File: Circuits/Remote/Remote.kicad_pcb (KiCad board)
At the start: 2 copper layers, 80 x 68.1 mm, 31 parts, among them P1 WRITER, Q1 2SK4017, SW1 WakeUp, U1 TWE_LITE_DIP, U2 STEPUPDIP3.3V, U3 ATP3011-PU, U4 HT82V739

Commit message: Assigned footprint.
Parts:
- removed P1: WRITER, SIL-6
- added CN1: WRITER, SIL-6, F.Cu at (31.8, 73.7)
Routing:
- net GND: track 0.00 -> 143.4 mm
- net /QGND: track 20.3 -> 161.5 mm
- net VCC: track 0.00 -> 119.7 mm
- net /SDA: track 0.00 -> 78.8 mm
- net /RESET#: track 0.00 -> 72.1 mm
- net /SCL: track 0.00 -> 68.1 mm
- net /3.3V: track 15.2 -> 82.8 mm
- net /SPK-: track 0.00 -> 45.3 mm
- net /SPK+: track 0.00 -> 44.6 mm
- net /RXD: track 0.00 -> 43.8 mm
- net /CFG: track 0.00 -> 40.0 mm
- net N-000004: track 0.00 -> 39.5 mm
- net N-0000050: track 0.00 -> 37.5 mm
- net /RST: track 0.00 -> 35.6 mm
- net /PRG: track 0.00 -> 34.2 mm
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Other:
- net class power added: clearance 0.254, trace_width 0.508, via_dia 0.889, via_drill 0.635

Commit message: Consider NTH.
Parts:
- added PB-SGM-135: VAL**, PB-SGM-135, F.Cu at (57.1, 45.1)
- added R11: 10k, R4, F.Cu at (45.7, 58.4)
- RV1, RV2: footprint POT_CMS -> RV2
- moved SW1 41.9 mm to (36.8, 19.1), turned to 180 degrees
- moved BT1 34.1 mm to (99.1, 61.0), turned to 270 degrees
- moved C4 23.4 mm to (91.4, 53.3), turned to 0 degrees
- moved U4 13.7 mm to (91.4, 44.5)
- moved C6 12.7 mm to (91.4, 33.0)
- moved U1 10.2 mm to (33.0, 47.0)
- moved SP1 10.2 mm to (66.0, 19.1)
- moved C5 10.2 mm to (81.2, 69.3)
- moved LD1 10.2 mm to (45.6, 41.4)
- moved LD2 10.2 mm to (53.2, 41.4)
- moved LD3 10.2 mm to (60.8, 41.4)
- moved R1 10.2 mm to (45.6, 36.3)
- moved R2 10.2 mm to (53.2, 36.3)
- moved R3 10.2 mm to (60.8, 36.3)
- moved R4 10.2 mm to (53.2, 61.7)
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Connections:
- net N-000001 renamed /V0
- net N-0000021 renamed /LPF2
- net N-0000022 renamed /LPF1
- net N-0000023 renamed /AOUT
- net N-0000025 renamed /VOL
- net N-0000027 renamed /PLAY#
- net N-0000029 renamed /VREF
- net N-000003 renamed /PWM4
- net N-0000030 renamed /AudioIn
- net N-0000031 renamed /PWM2
- net N-000004 renamed /3V_Gate
- net N-000005 renamed /LD1
- net N-0000050 renamed /PWM1
- net N-000006 renamed /LD2
- net N-000007 renamed /LD3
- net N-000009 renamed /G
- R10 pad 2: N-0000020 -> /LPF3
- RV2 pad 1: /QGND -> /LPF3
- RV2 pad 3: N-0000020 -> /QGND
- SW1 pad 1: /WUP -> N-0000016
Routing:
- net N-0000016: track 0.00 -> 37.4 mm
- net /PLAY#: track 14.8 -> 31.0 mm
- net /LPF3: track 0.00 -> 12.0 mm
- net /AudioIn: track 19.2 -> 8.67 mm
- net GND: track 143.4 -> 132.9 mm
- net /SPK-: track 45.3 -> 36.8 mm
- net /QGND: track 161.5 -> 153.3 mm
- net /VREF: track 23.7 -> 30.7 mm
- net /RESET#: track 72.1 -> 77.9 mm
- net /3.3V: track 82.8 -> 77.1 mm
- net N-0000020: track 4.93 -> 0.00 mm
- net /VOL: track 11.6 -> 6.88 mm
- net /V0: track 16.5 -> 20.2 mm
- net /3V_Gate: track 39.5 -> 35.8 mm
- net /LPF1: track 16.3 -> 12.7 mm
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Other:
- board size 80 x 68.1 mm -> 90 x 66 mm

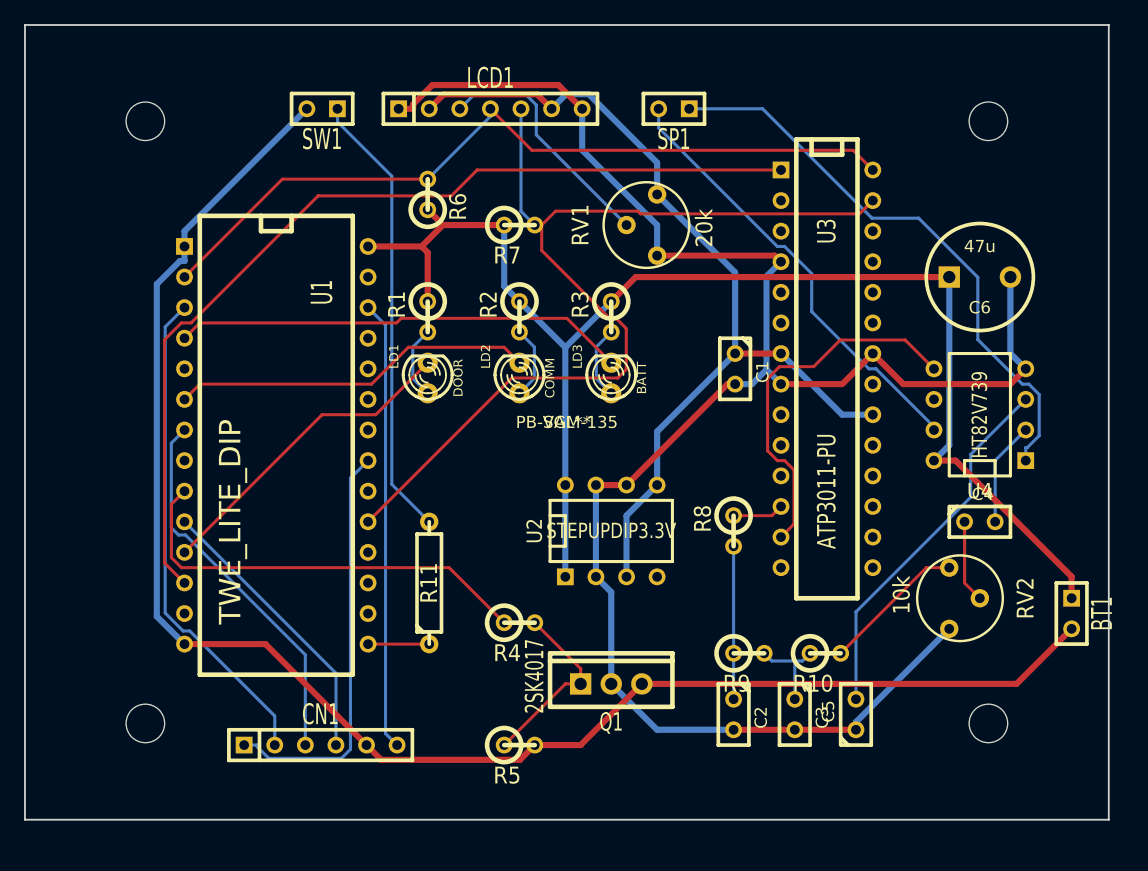
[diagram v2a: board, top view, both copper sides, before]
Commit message: Modified parts layout.
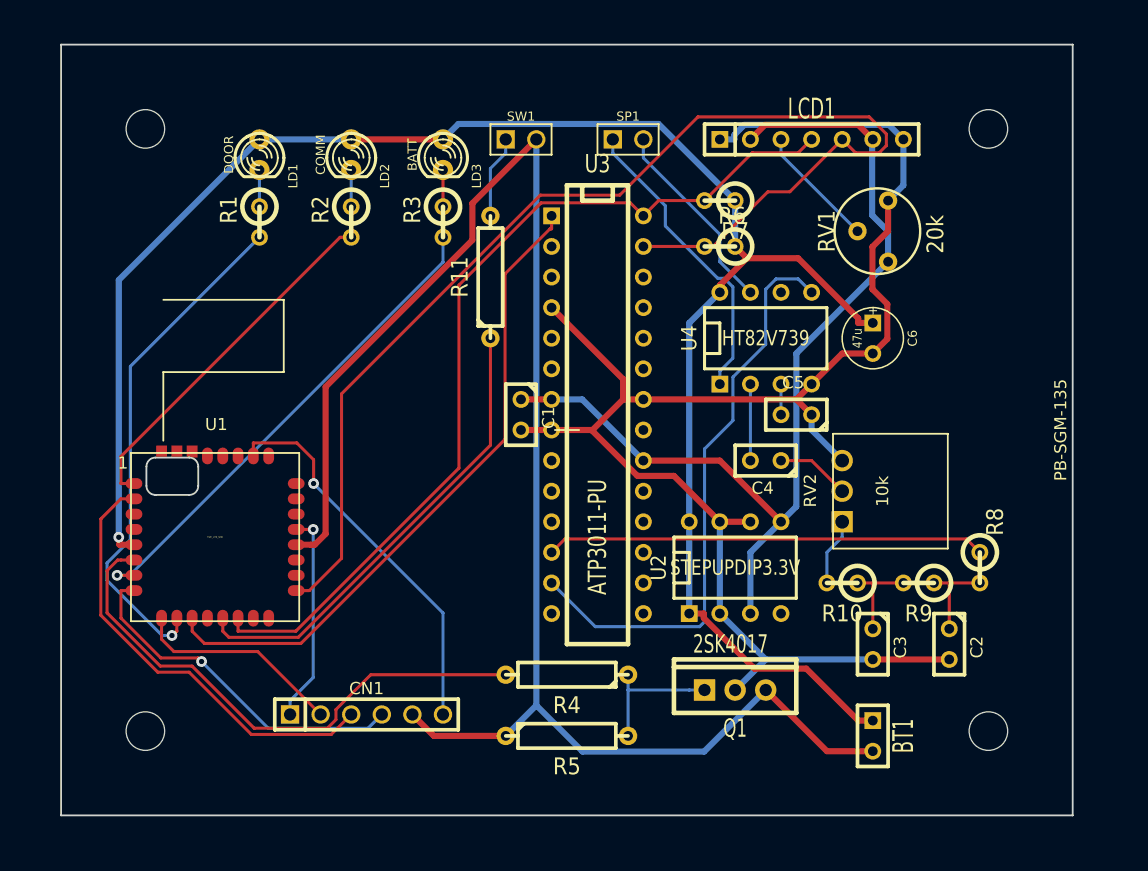
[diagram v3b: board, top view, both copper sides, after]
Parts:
- C6: footprint C2V8 -> C1V5
- CN1: footprint SIL-6 -> PIN_ARRAY-6X1
- R4, R5: footprint R1 -> R4
- RV2: footprint RV2 -> TSR-3386T
- SP1, SW1: footprint SIL-2 -> PIN_ARRAY_2X1
- U1: value TWE_LITE_DIP -> TWE_LITE_SMD; footprint DIP-28__600 -> TWE-001L-SMD
- moved LCD1 26.8 mm to (77.5, 21.6)
- moved R11 25.9 mm to (50.8, 33.0)
- moved C5 25.4 mm to (76.2, 44.5), turned to 180 degrees
- moved R6 24.6 mm to (69.8, 30.5), turned to 180 degrees
- moved LD1 23.2 mm to (31.6, 22.9), turned to 270 degrees
- moved LD2 23.2 mm to (39.2, 22.9), turned to 270 degrees
- moved LD3 23.2 mm to (46.9, 22.9), turned to 270 degrees
- moved R8 20.7 mm to (91.4, 57.1)
- moved U3 19.4 mm to (59.7, 44.5)
- moved BT1 19.4 mm to (82.5, 71.1)
- moved RV1 19.2 mm to (82.5, 29.2)
- moved U4 18.9 mm to (73.7, 38.1), turned to 0 degrees
- moved C2 18.8 mm to (88.9, 63.5)
- moved C4 18.5 mm to (73.7, 48.3), turned to 180 degrees
- moved C1 18.2 mm to (53.3, 44.5)
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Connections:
- net /CFG renamed /M2
- net N-0000016 renamed /SW
- C1 pad 1: /3.3V -> /3.3VOUT
- LCD1 pad 2: /3.3V -> /3.3VOUT
- LCD1 pad 6: /3.3V -> /3.3VOUT
- LD1 pad 1: /LD1 -> VCC
- LD1 pad 2: /PWM4 -> /LD1
- LD2 pad 1: /LD2 -> VCC
- LD2 pad 2: /PWM2 -> /LD2
- LD3 pad 1: /LD3 -> VCC
- LD3 pad 2: /PWM1 -> /LD3
- Q1 pad G: /G -> /Gate
- R1 pad 1: VCC -> /LD1
- R1 pad 2: /LD1 -> /PWM4
- R2 pad 1: VCC -> /LD2
- R2 pad 2: /LD2 -> /PWM2
- R3 pad 1: VCC -> /LD3
- R3 pad 2: /LD3 -> /PWM1
- R4 pad 1: /3V_Gate -> /Gate
- R4 pad 2: /G -> /GND_SW
- R5 pad 1: /G -> GND
- R5 pad 2: GND -> /Gate
- R6 pad 2: /SCL -> /SDA
- R7 pad 2: /SDA -> /SCL
- RV1 pad 1: /QGND -> /3.3VOUT
- RV1 pad 3: /3.3V -> /QGND
- U1 pad 1: GND -> /PWM2
- U1 pad 10: /TXD -> /PWM4
- U1 pad 11: /PWM4 -> /RESET#
- U1 pad 12: /RESET# -> (no net)
- U1 pad 13: (no net) -> /WUP
- U1 pad 14: GND -> /SCL
- U1 pad 15: /WUP -> (no net)
- U1 pad 17: (no net) -> /SDA
- U1 pad 19: /SDA -> (no net)
- U1 pad 2: /SCL -> /PRG
- U1 pad 20: (no net) -> GND
- U1 pad 28: VCC -> (no net)
- U1 pad 3: /RXD -> (no net)
- U1 pad 4: /PWM1 -> (no net)
- U1 pad 5: (no net) -> VCC
- U1 pad 6: /PWM2 -> /GND_SW
- U1 pad 7: /PRG -> /PWM1
- U1 pad 8: (no net) -> /TXD
- U1 pad 9: /3V_Gate -> /RXD
- U2 pad 3: /3.3V -> /3.3VOUT
- U2 pad 5: /3.3V -> /3.3VOUT
- U3 pad 20: /3.3V -> /3.3VOUT
- U3 pad 7: /3.3V -> /3.3VOUT
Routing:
- net /3.3VOUT: track 0.00 -> 81.6 mm
- net /3.3V: track 77.1 -> 0.00 mm
- net /GND_SW: track 0.00 -> 45.5 mm
- net /3V_Gate: track 35.8 -> 0.00 mm
- net /WUP: track 5.08 -> 39.0 mm
- net VCC: track 117.2 -> 151.1 mm, vias 0 -> 1
- net /AOUT: track 4.25 -> 36.5 mm
- net /SW: track 37.4 -> 6.88 mm
- net /VREF: track 30.7 -> 2.54 mm
- net /RXD: track 41.1 -> 17.5 mm
- net /RESET#: track 77.9 -> 54.7 mm
- net /SPK+: track 47.9 -> 25.2 mm
- net /SPK-: track 36.8 -> 16.4 mm
- net /QGND: track 153.3 -> 133.0 mm
- net /SDA: track 81.1 -> 99.4 mm
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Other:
- board size 90 x 66 mm -> 84 x 64 mm

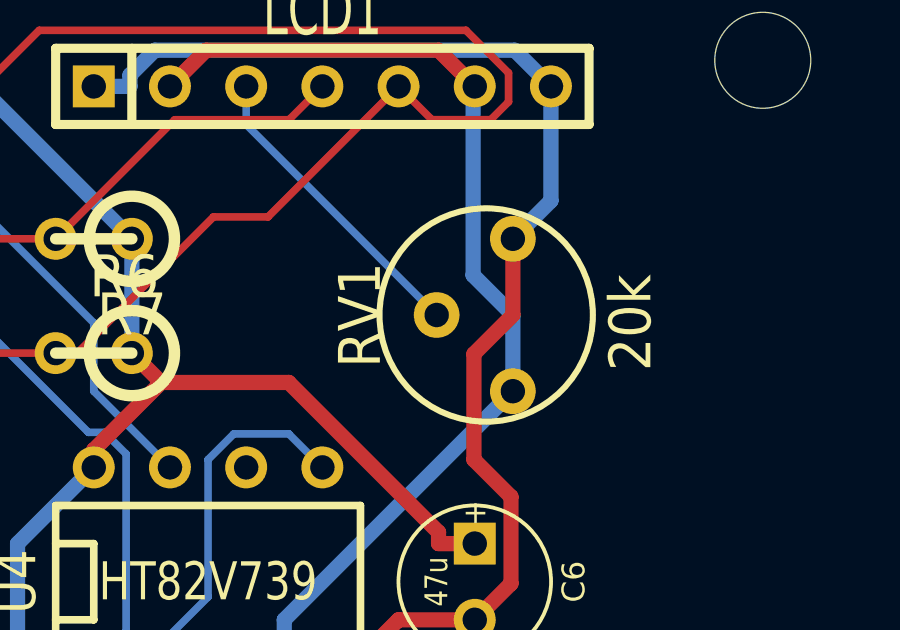
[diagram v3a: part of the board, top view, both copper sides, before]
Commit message: Replaced RV2 to RV-3362P.
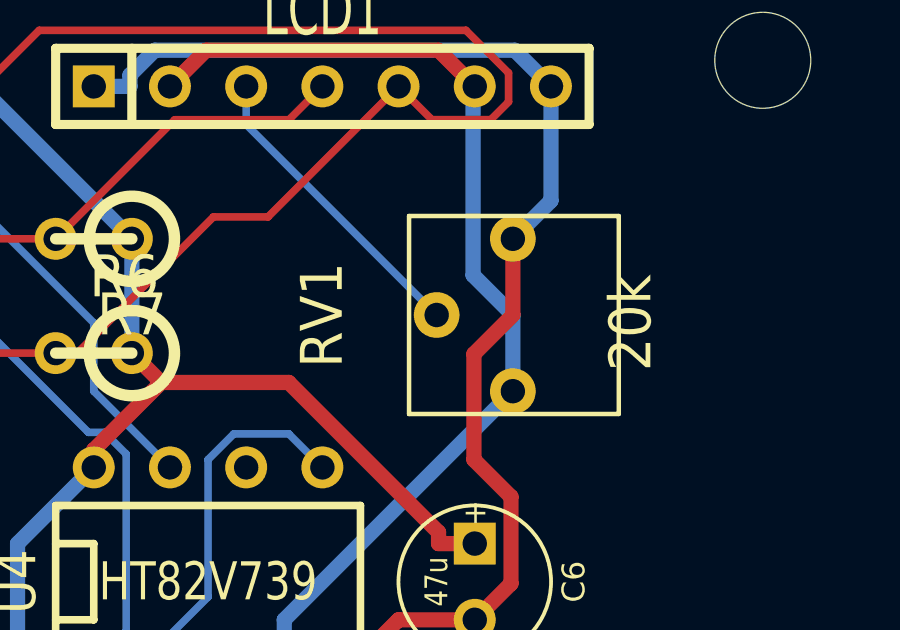
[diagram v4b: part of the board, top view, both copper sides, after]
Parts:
- RV1: footprint RV2 -> RV-3362P
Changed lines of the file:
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@@
-    )
-  )
-  (module RV2 (layer F.Cu)
-    (at 82.55 29.21 90)
-    (descr "Resistance variable / potentiometre")
-    (tags R)
-    (autoplace_cost90 10)
-    (autoplace_cost180 10)
-    (fp_text reference RV1 (at 0 -3.81 90) (layer F.SilkS)
-      (effects (font (size 1.397 1.27) (thickness 0.2032)))
-    )
-    (fp_text value 20k (at -0.254 5.207 90) (layer F.SilkS)
-      (effects (font (size 1.397 1.27) (thickness 0.2032)))
-    )
-    (fp_circle (center 0 0.381) (end 0 -3.175) (layer F.SilkS) (width 0.2032))
-    (pad 1 thru_hole circle (at -2.54 1.27 90) (size 1.524 1.524) (drill 0.8128)
-      (layers *.Cu *.Mask F.SilkS)
-      (net 1 /3.3VOUT)
-    )
-    (pad 2 thru_hole circle (at 0 -1.27 90) (size 1.524 1.524) (drill 0.8128)
-      (layers *.Cu *.Mask F.SilkS)
-      (net 28 /V0)
-    )
-    (pad 3 thru_hole circle (at 2.54 1.27 90) (size 1.524 1.524) (drill 0.8128)
-      (layers *.Cu *.Mask F.SilkS)
-      (net 18 /QGND)
-    )
-    (model discret/adjustable_rx2.wrl
-      (at (xyz 0 0 0))
-      (scale (xyz 1 1 1))
-      (rotate (xyz 0 0 0))
     )
   )
@@
       (rotate (xyz 0 0 0))
     )
+  )
+  (module RV-3362P (layer F.Cu)
+    (at 82.55 29.21 90)
+    (descr "Resistance variable / potentiometre")
+    (tags R)
+    (autoplace_cost90 10)
+    (autoplace_cost180 10)
+    (fp_text reference RV1 (at 0 -5.08 90) (layer F.SilkS)
+      (effects (font (size 1.397 1.27) (thickness 0.2032)))
+    )
+    (fp_text value 20k (at -0.254 5.207 90) (layer F.SilkS)
+      (effects (font (size 1.397 1.27) (thickness 0.2032)))
+    )
+    (fp_line (start -3.3 -2.19) (end -3.3 4.8) (layer F.SilkS) (width 0.15))
+    (fp_line (start -3.3 4.8) (end 3.3 4.8) (layer F.SilkS) (width 0.15))
+    (fp_line (start 3.3 4.8) (end 3.3 -2.19) (layer F.SilkS) (width 0.15))
+    (fp_line (start 3.3 -2.19) (end -3.3 -2.19) (layer F.SilkS) (width 0.15))
+    (pad 1 thru_hole circle (at -2.54 1.27 90) (size 1.524 1.524) (drill 0.8128)
+      (layers *.Cu *.Mask F.SilkS)
+      (net 1 /3.3VOUT)
+    )
+    (pad 2 thru_hole circle (at 0 -1.27 90) (size 1.524 1.524) (drill 0.8128)
+      (layers *.Cu *.Mask F.SilkS)
+      (net 28 /V0)
+    )
+    (pad 3 thru_hole circle (at 2.54 1.27 90) (size 1.524 1.524) (drill 0.8128)
+      (layers *.Cu *.Mask F.SilkS)
+      (net 18 /QGND)
+    )
+    (model discret/adjustable_rx2.wrl
+      (at (xyz 0 0 0))
+      (scale (xyz 1 1 1))
+      (rotate (xyz 0 0 0))
+    )

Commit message: Renamed RV-TSR-3386T.
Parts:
- RV2: footprint TSR-3386T -> RV-TSR-3386T
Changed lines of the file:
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@@
     (descr "8 pins DIL package, round pads")
     (tags DIL)
-    (fp_text reference U2 (at -6.35 0 90) (layer F.SilkS)
+    (fp_text reference U2 (at 6.35 -1.27 90) (layer F.SilkS)
       (effects (font (size 1.27 1.143) (thickness 0.2032)))
     )
@@
     (descr "28 pins DIL package, round pads, width 300mil")
     (tags DIL)
-    (fp_text reference U3 (at -20.828 0 360) (layer F.SilkS)
+    (fp_text reference U3 (at -20.32 0 360) (layer F.SilkS)
       (effects (font (size 1.524 1.143) (thickness 0.3048)))
     )
@@
     (descr "Condensateur e = 1 pas")
     (tags C)
-    (fp_text reference C1 (at 0.254 -2.286 270) (layer F.SilkS)
+    (fp_text reference C1 (at 0 2.54 270) (layer F.SilkS)
       (effects (font (size 1.016 1.016) (thickness 0.2032)))
     )
@@
     (autoplace_cost90 10)
     (autoplace_cost180 10)
-    (fp_text reference R6 (at -1.016 2.54 180) (layer F.SilkS)
+    (fp_text reference R6 (at -3.81 3.81 180) (layer F.SilkS)
       (effects (font (size 1.397 1.27) (thickness 0.2032)))
     )
@@
     (autoplace_cost90 10)
     (autoplace_cost180 10)
-    (fp_text reference R7 (at -1.27 -2.54 180) (layer F.SilkS)
+    (fp_text reference R7 (at -3.81 -3.81 180) (layer F.SilkS)
       (effects (font (size 1.397 1.27) (thickness 0.2032)))
     )
@@
       (scale (xyz 1 1 1))
       (rotate (xyz 0 0 0))
-    )
-  )
-  (module TSR-3386T (layer F.Cu)
-    (at 80.01 50.8)
-    (descr "Square Trimming Potentiometer")
-    (tags TSR-3386T)
-    (fp_text reference RV2 (at -2.65 -0.05 90) (layer F.SilkS)
-      (effects (font (size 1.016 1.016) (thickness 0.2032)))
-    )
-    (fp_text value 10k (at 3.35 0 90) (layer F.SilkS)
-      (effects (font (size 1.016 1.016) (thickness 0.2032)))
-    )
-    (fp_line (start -0.76 -4.765) (end 8.77 -4.765) (layer F.SilkS) (width 0.15))
-    (fp_line (start 8.77 -4.765) (end 8.77 4.765) (layer F.SilkS) (width 0.15))
-    (fp_line (start 8.77 4.765) (end -0.76 4.765) (layer F.SilkS) (width 0.15))
-    (fp_line (start -0.76 4.765) (end -0.76 -4.765) (layer F.SilkS) (width 0.15))
-    (pad 1 thru_hole rect (at 0 2.54) (size 1.778 1.778) (drill 1.143)
-      (layers *.Cu *.Mask F.SilkS)
-      (net 11 /LPF3)
-    )
-    (pad 3 thru_hole circle (at 0 -2.54) (size 1.778 1.778) (drill 1.143)
-      (layers *.Cu *.Mask F.SilkS)
-      (net 18 /QGND)
-    )
-    (pad 2 thru_hole circle (at 0 0) (size 1.778 1.778) (drill 1.143)
-      (layers *.Cu *.Mask F.SilkS)
-      (net 29 /VOL)
     )
   )
@@
     (autoplace_cost90 10)
     (autoplace_cost180 10)
-    (fp_text reference RV1 (at 0 -5.08 90) (layer F.SilkS)
-      (effects (font (size 1.397 1.27) (thickness 0.2032)))
-    )
-    (fp_text value 20k (at -0.254 5.207 90) (layer F.SilkS)
+    (fp_text reference RV1 (at 0 6.35 90) (layer F.SilkS)
+      (effects (font (size 1.397 1.27) (thickness 0.2032)))
+    )
+    (fp_text value 20k (at 0 3.81 90) (layer F.SilkS)
       (effects (font (size 1.397 1.27) (thickness 0.2032)))
     )
@@
     )
   )
+  (module RV-TSR-3386T (layer F.Cu)
+    (at 80.01 50.8)
+    (descr "Square Trimming Potentiometer")
+    (tags TSR-3386T)
+    (fp_text reference RV2 (at 10.16 0 90) (layer F.SilkS)
+      (effects (font (size 1.016 1.016) (thickness 0.2032)))
+    )
+    (fp_text value 10k (at 3.35 0 90) (layer F.SilkS)
+      (effects (font (size 1.016 1.016) (thickness 0.2032)))
+    )
+    (fp_line (start -0.76 -4.765) (end 8.77 -4.765) (layer F.SilkS) (width 0.15))
+    (fp_line (start 8.77 -4.765) (end 8.77 4.765) (layer F.SilkS) (width 0.15))
+    (fp_line (start 8.77 4.765) (end -0.76 4.765) (layer F.SilkS) (width 0.15))
+    (fp_line (start -0.76 4.765) (end -0.76 -4.765) (layer F.SilkS) (width 0.15))
+    (pad 1 thru_hole rect (at 0 2.54) (size 1.778 1.778) (drill 1.143)
+      (layers *.Cu *.Mask F.SilkS)
+      (net 11 /LPF3)
+    )
+    (pad 3 thru_hole circle (at 0 -2.54) (size 1.778 1.778) (drill 1.143)
+      (layers *.Cu *.Mask F.SilkS)
+      (net 18 /QGND)
+    )
+    (pad 2 thru_hole circle (at 0 0) (size 1.778 1.778) (drill 1.143)
+      (layers *.Cu *.Mask F.SilkS)
+      (net 29 /VOL)
+    )
+  )
